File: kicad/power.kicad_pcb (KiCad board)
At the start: 2 copper layers, 84.1 x 61.7 mm, 99 parts, among them J4 Bus_PCI_Express_x1, J5 Conn_01x02_Pin, J6 USB_C_Receptacle_USB2.0_16P, J7 Conn_01x03, Q1 AO3400A, Q2 AO3400A, U1 MP2672GD-0000-Z, U2 MP2236CGJ-P, U3 MP2236CGJ-P, U5 W25Q128JVP, U6 MCP25625T-E/ML, U7 RP2040, X1 ABM8-272-T3, Y1 X322516MLB4SI

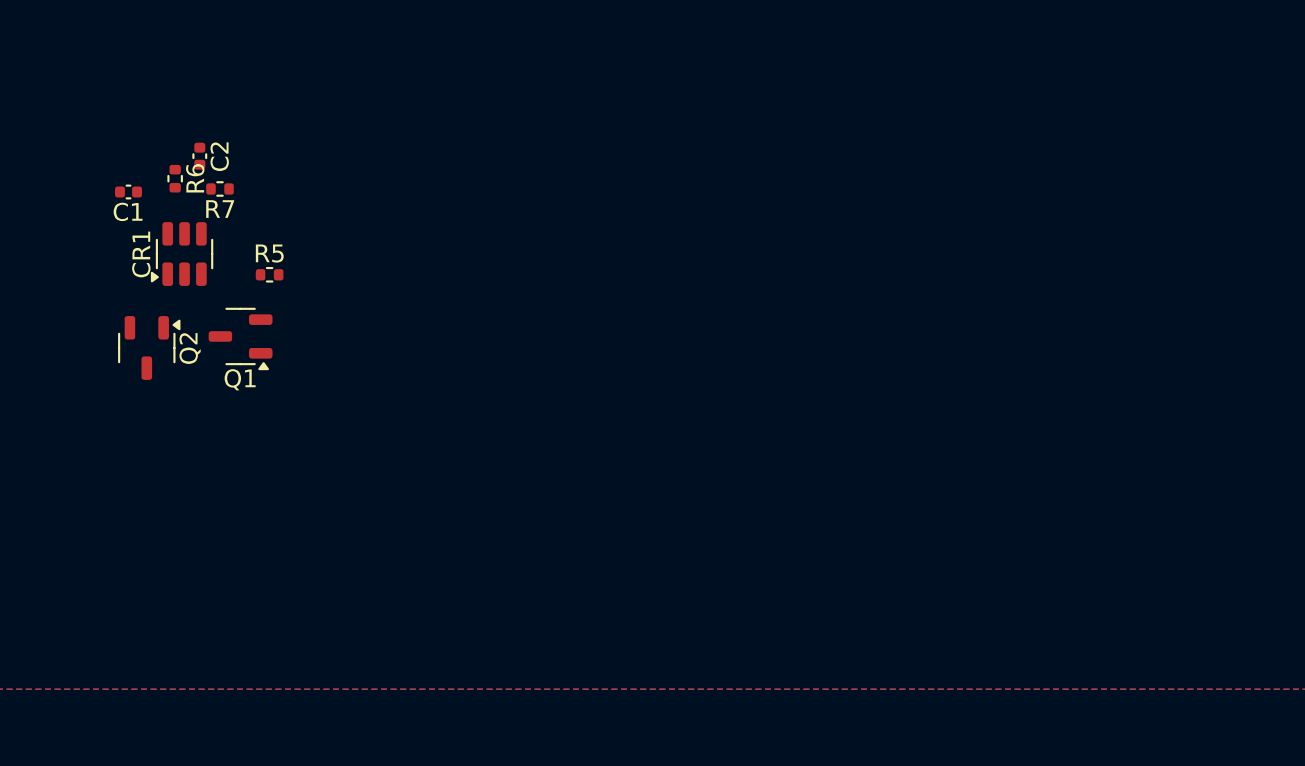
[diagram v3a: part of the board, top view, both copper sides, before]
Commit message: Update FETs and Protection IC
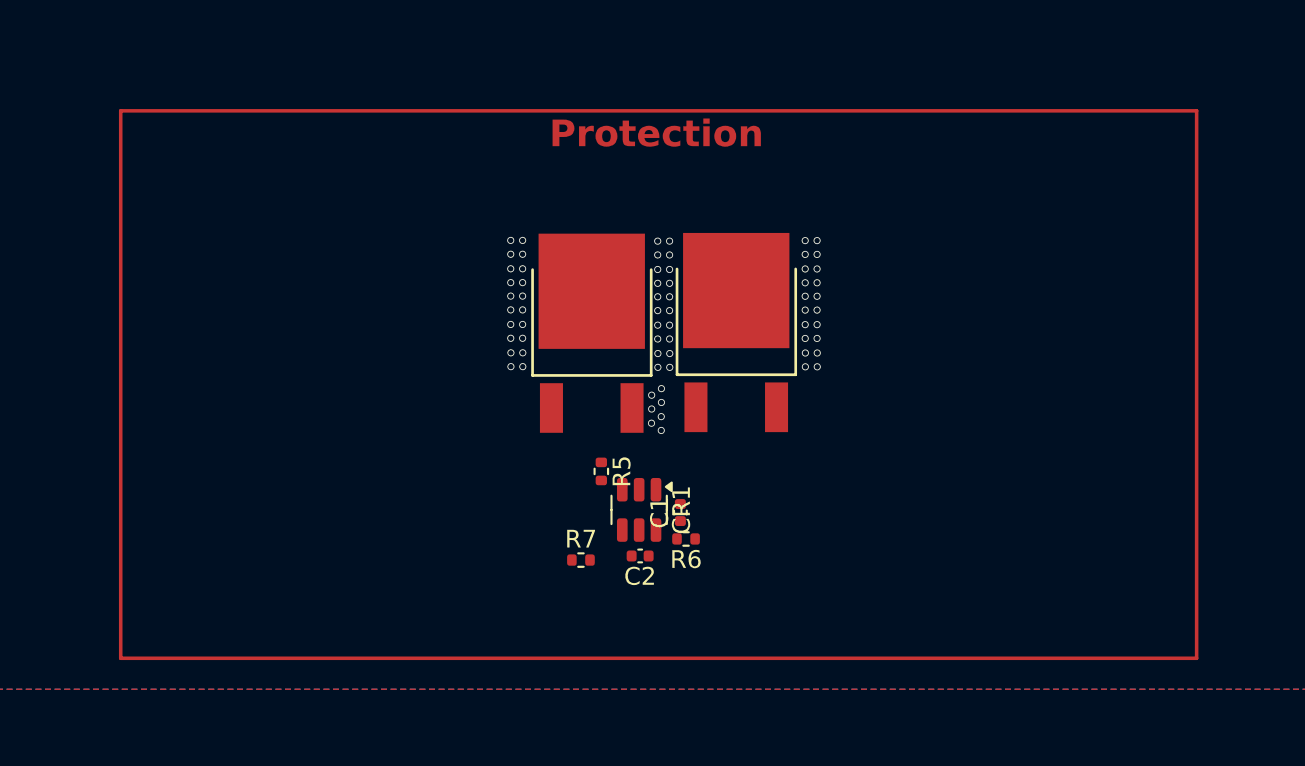
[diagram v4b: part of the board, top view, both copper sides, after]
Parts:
- CR1: value S-8252AAL-M6T1U -> HY2120-CB
- Q1, Q2: value AO3400A -> NCE3080K; footprint Package_TO_SOT_SMD:SOT-23-3 -> POWERLIB:TO-252-2_L6.6-W6.1-P4.57-LS9.9-TL-CW
- moved C1 36.0 mm to (164.6, 35.9), turned to 90 degrees
- moved R6 35.3 mm to (165.0, 37.4), turned to 180 degrees
- moved C2 33.6 mm to (162.4, 38.4), turned to 180 degrees
- moved Q2 33.3 mm to (167.8, 26.7), turned to 90 degrees
- moved CR1 29.4 mm to (162.3, 35.8), turned to -90 degrees
- moved R7 29.2 mm to (159.0, 38.6), turned to 0 degrees
- moved R5 21.8 mm to (160.2, 33.6), turned to -90 degrees
- moved Q1 19.8 mm to (159.6, 26.7), turned to 90 degrees
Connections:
- Q1 pad 1: unconnected-(Q1-G-Pad1) -> Net-(CR1-CO)
- Q1 pad 2: LOAD_GND -> FET
- Q1 pad 3: Net-(CR1-CO) -> LOAD_GND
- Q2 pad 2: B_GND -> FET
- Q2 pad 3: Net-(CR1-CO) -> B_GND
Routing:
- net GND: vias 171 -> 238
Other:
- board text added: "Protection"

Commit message: Prototype BMS and Protection
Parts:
- removed R7: 470R, Resistor_SMD:R_0402_1005Metric
- added R1: 470R, Resistor_SMD:R_1206_3216Metric, F.Cu at (261.0, 79.9)
- C1, C15, C16, C2, C20, C23, C26: footprint Capacitor_SMD:C_0402_1005Metric -> Capacitor_SMD:C_0603_1608Metric
- C12, C13, C14, C17, C18, C19, C21, C22, C24: footprint Capacitor_SMD:C_0402_1005Metric -> Capacitor_SMD:C_0805_2012Metric
- C25: footprint Capacitor_SMD:C_0402_1005Metric -> Capacitor_SMD:C_1206_3216Metric
- R11, R17, R23, R6: footprint Resistor_SMD:R_0402_1005Metric -> Resistor_SMD:R_1206_3216Metric
- R12, R13, R14, R16, R18, R19, R20, R21, R5: footprint Resistor_SMD:R_0402_1005Metric -> Resistor_SMD:R_0603_1608Metric
- R15, R24: footprint Resistor_SMD:R_0402_1005Metric -> Resistor_SMD:R_0805_2012Metric
- moved TP2 234.3 mm to (316.4, 95.9)
- moved TP4 234.3 mm to (316.4, 100.5)
- moved TP5 234.3 mm to (316.4, 105.1)
- moved TP6 234.3 mm to (316.4, 109.7)
- moved C13 191.6 mm to (251.2, 112.9)
- moved C14 191.0 mm to (253.3, 113.0), turned to -90 degrees
- moved C12 188.4 mm to (249.3, 112.9)
- moved C19 186.9 mm to (250.0, 118.9)
- moved C18 186.2 mm to (248.0, 118.9)
- moved C17 185.6 mm to (246.0, 118.9)
- moved C15 184.4 mm to (257.5, 109.7)
- moved U3 184.3 mm to (258.3, 112.4)
- moved L2 184.0 mm to (255.3, 122.5), turned to 180 degrees
- moved C16 183.3 mm to (260.5, 120.2)
- moved R11 183.2 mm to (260.8, 116.7)
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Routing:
- net VCC: track 0.00 -> 40.0 mm, vias 0 -> 3
- net +3.3V OUT: track 0.00 -> 36.7 mm, vias 0 -> 42
- net +4.2V: track 0.00 -> 31.5 mm, vias 0 -> 8
- net LOAD_GND: track 0.00 -> 30.4 mm, vias 0 -> 92
- net VIN: track 0.00 -> 30.0 mm, vias 0 -> 2
- net +8.4V: track 0.00 -> 19.6 mm, vias 0 -> 23
- net (no net): track 34.7 -> 53.6 mm, vias 3 -> 7
- net Net-(U1-MID): track 0.00 -> 15.7 mm
- net Net-(CR1-CO): track 0.00 -> 15.4 mm, vias 0 -> 2
- net Net-(D4-K): track 0.00 -> 9.49 mm, vias 0 -> 2
- net FET: track 0.00 -> 8.83 mm
- net B_GND: track 0.00 -> 7.67 mm
- net Net-(U1-NTC): track 0.00 -> 7.34 mm
- net FB2: track 0.00 -> 6.56 mm
- net Net-(C26-Pad1): track 0.00 -> 6.06 mm
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- added copper zone on B.Cu, net +3.3V OUT
- added copper zone on F.Cu, net +3.3V OUT
- added copper zone on F.Cu, net +4.2V
- added copper zone on B.Cu, net +8.4V
- added copper zone on F.Cu, net +8.4V
- added copper zone on F.Cu, net B_GND
- added copper zone on B.Cu, net LOAD_GND
- added copper zone on F.Cu, net LOAD_GND
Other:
- board size 84.1 x 61.7 mm -> 169.4 x 98.2 mm
- board text removed: "Protection"

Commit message: Fixing Zones
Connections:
- net Net-(C26-Pad1) renamed L3P2
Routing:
- added copper zone on B.Cu, net +4.2V
- added copper zone on F.Cu, net L3P2
- added copper zone on F.Cu, net SW2
- added copper zone on F.Cu, net VIN

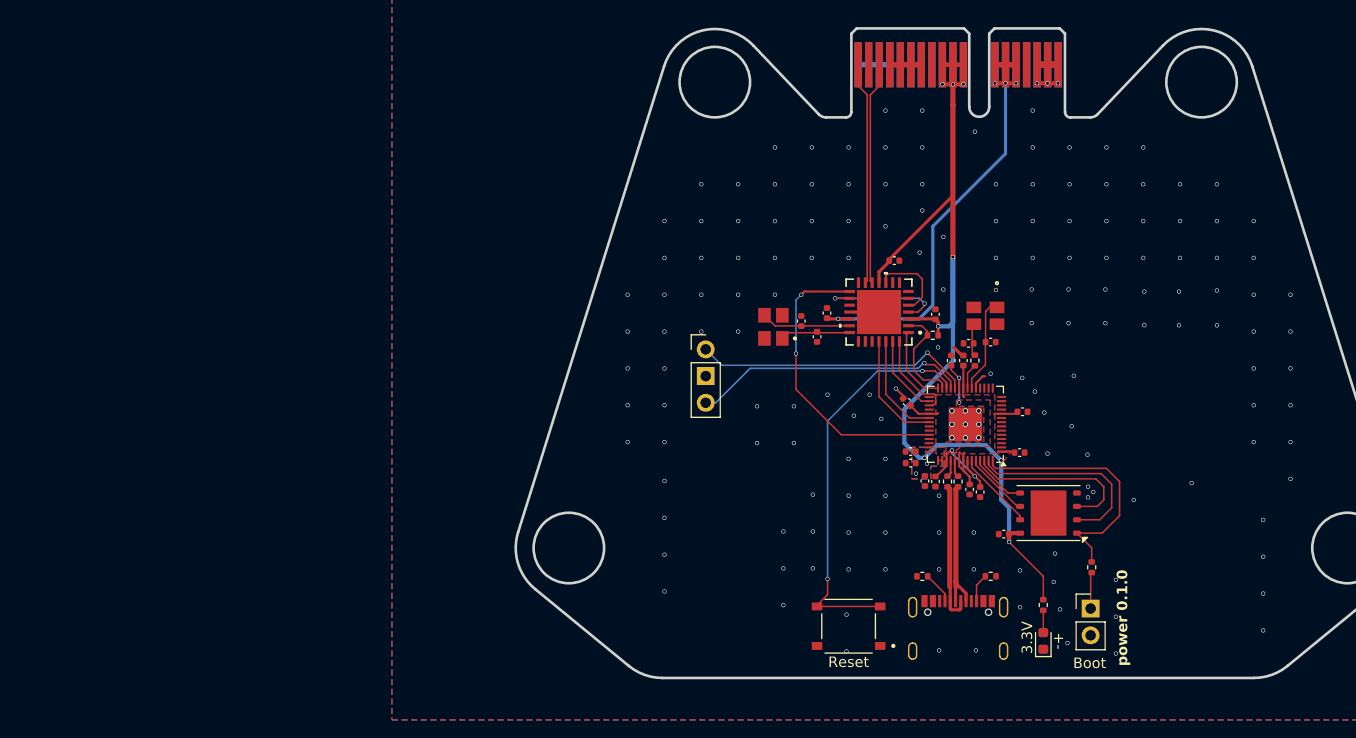
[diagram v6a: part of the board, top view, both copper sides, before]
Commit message: Move MCU to the side
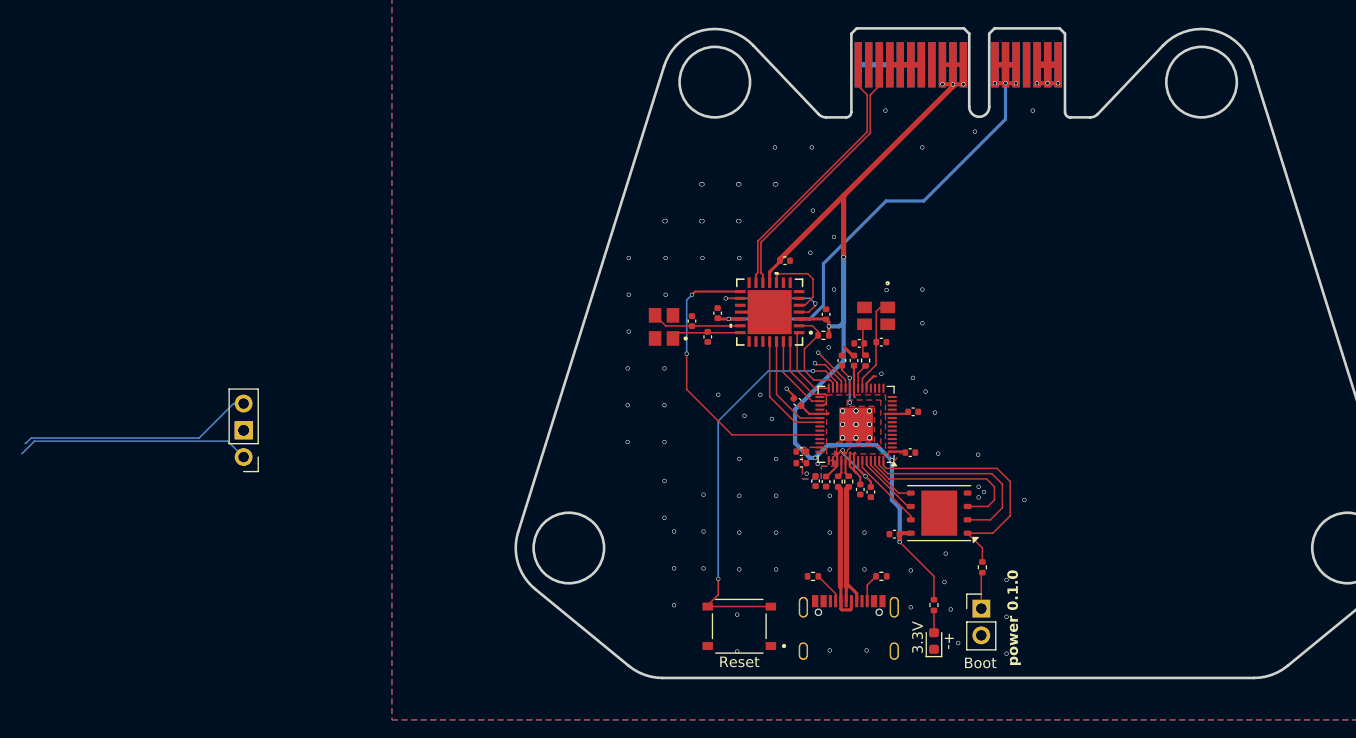
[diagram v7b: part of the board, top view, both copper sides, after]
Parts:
- added ?: , , F.Cu at (78.5, 98.9)
- moved J7 45.1 mm to (78.5, 101.4), turned to 180 degrees
- moved C32 10.4 mm to (133.9, 87.9)
- moved C41 10.4 mm to (131.1, 96.2)
- moved C42 10.4 mm to (142.1, 97.1)
- moved C44 10.4 mm to (131.5, 100.9)
- moved C45 10.4 mm to (131.5, 102.0)
- moved U6 10.4 mm to (128.5, 87.6)
- moved C31 10.4 mm to (122.6, 90.0)
- moved C33 10.4 mm to (121.1, 88.5)
- moved C34 10.4 mm to (123.6, 87.7)
- moved S2 10.4 mm to (125.6, 117.5)
- moved Y1 10.4 mm to (118.5, 89.1)
- moved C27 10.4 mm to (139.1, 90.5)
- moved C28 10.4 mm to (137.0, 90.6)
- moved C29 10.4 mm to (140.4, 108.8)
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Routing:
- net +5V: track 43.2 -> 49.5 mm
- net CANN: track 21.1 -> 25.4 mm
- net CANP: track 21.1 -> 25.4 mm
- net +3.3V: track 112.4 -> 110.1 mm
- net GND: vias 171 -> 97
